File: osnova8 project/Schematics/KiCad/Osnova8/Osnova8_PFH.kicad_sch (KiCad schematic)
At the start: 14 parts, among them U26 74LS283, U27 74LS283, U28 74LS374, U29 74LS541, U30 74LS670, U31 74LS670, U32 74LS541

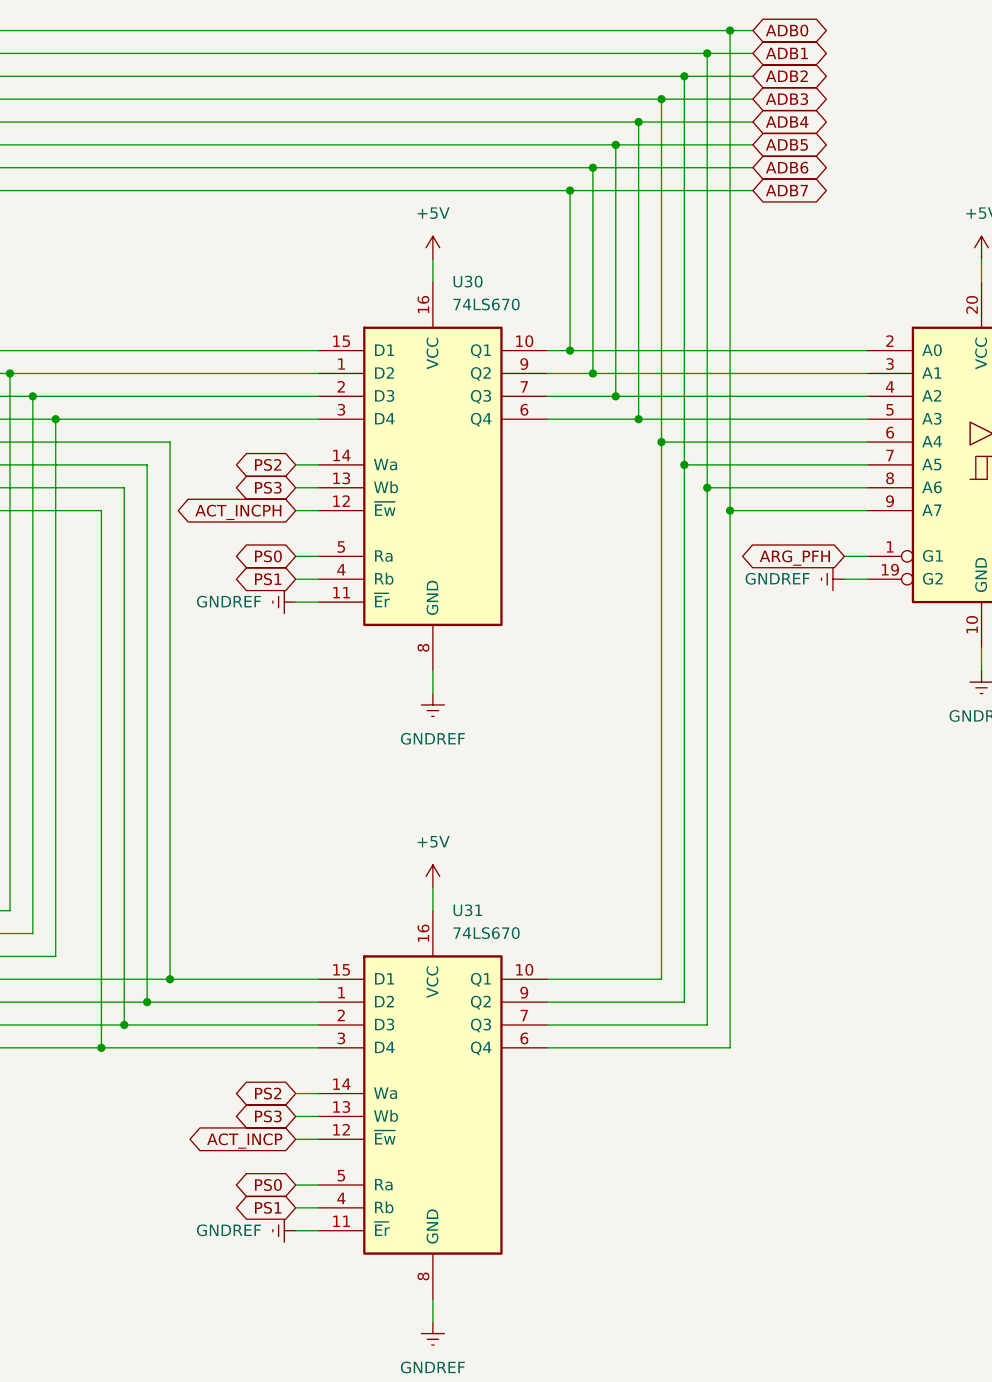
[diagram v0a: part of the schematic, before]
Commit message: updated schematics
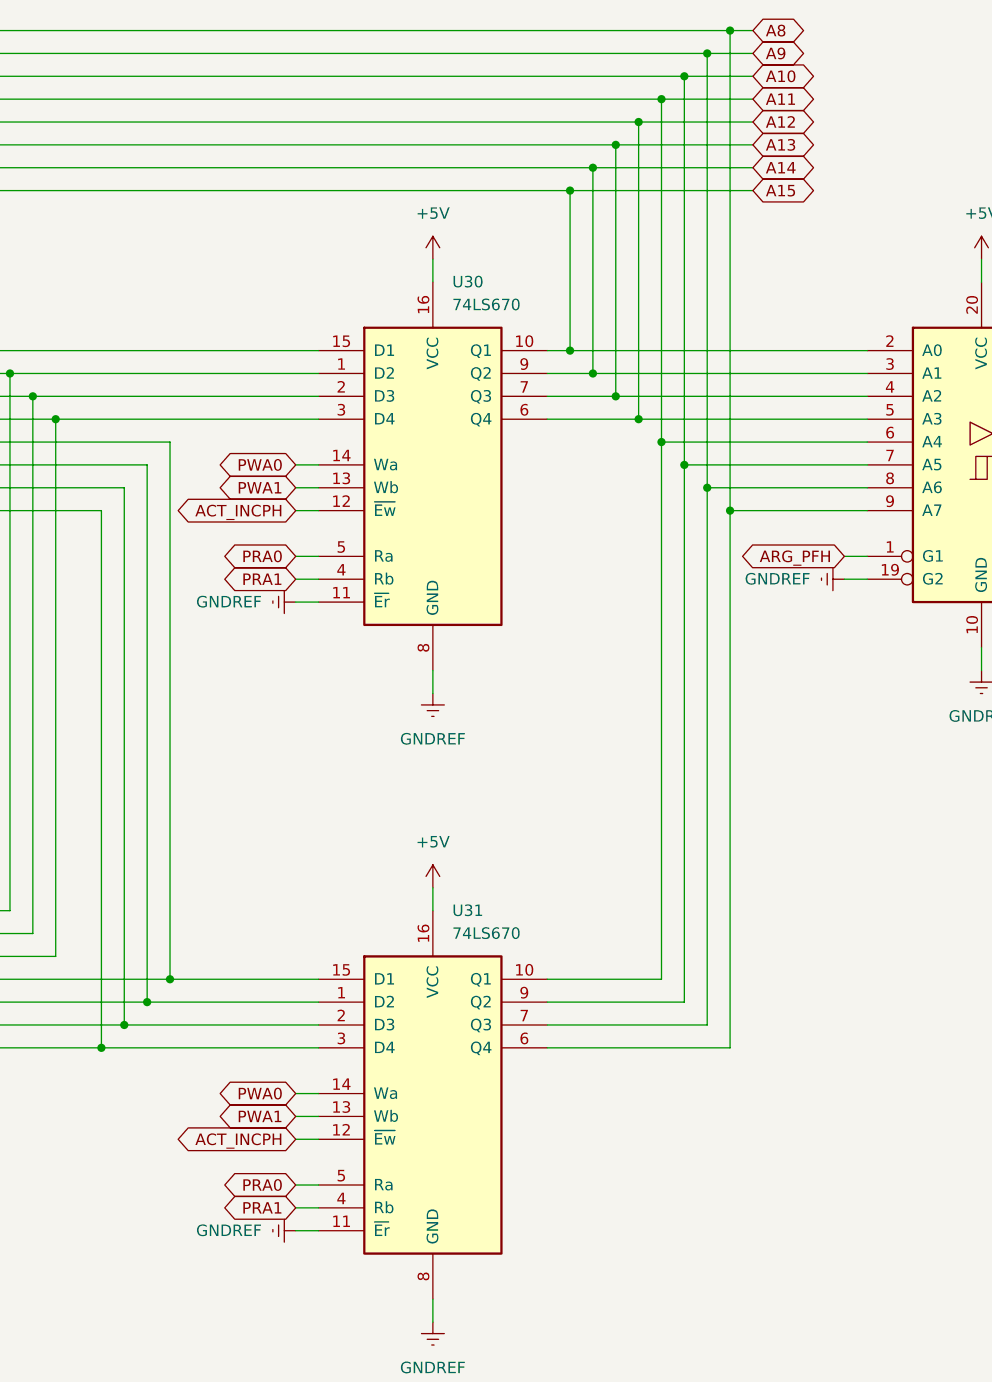
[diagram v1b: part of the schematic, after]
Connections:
- net ACT_INCP is gone; now on net ACT_INCPH: U31.12 (~{Ew})
- net ADB0 renamed A8
- net ADB1 renamed A9
- net ADB2 renamed A10
- net ADB3 renamed A11
- net ADB4 renamed A12
- net ADB5 renamed A13
- net ADB6 renamed A14
- net ADB7 renamed A15
- net PS0 renamed PRA0
- net PS1 renamed PRA1
- net PS2 renamed PWA0
- net PS3 renamed PWA1
